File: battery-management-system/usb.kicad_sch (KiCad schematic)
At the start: 20 parts, among them J14 AMPHENOL_micro_usb_10118194-0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, U6 FT230XS

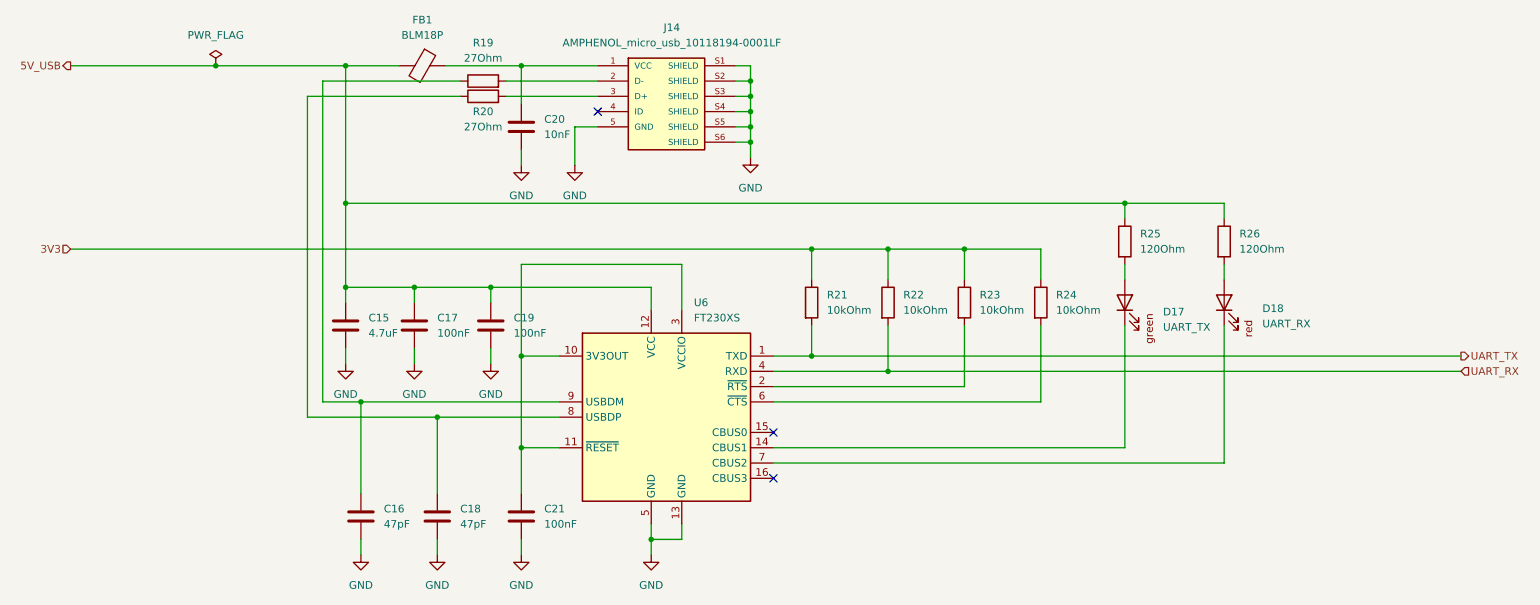
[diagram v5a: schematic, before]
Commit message: add enable input for cell measurement
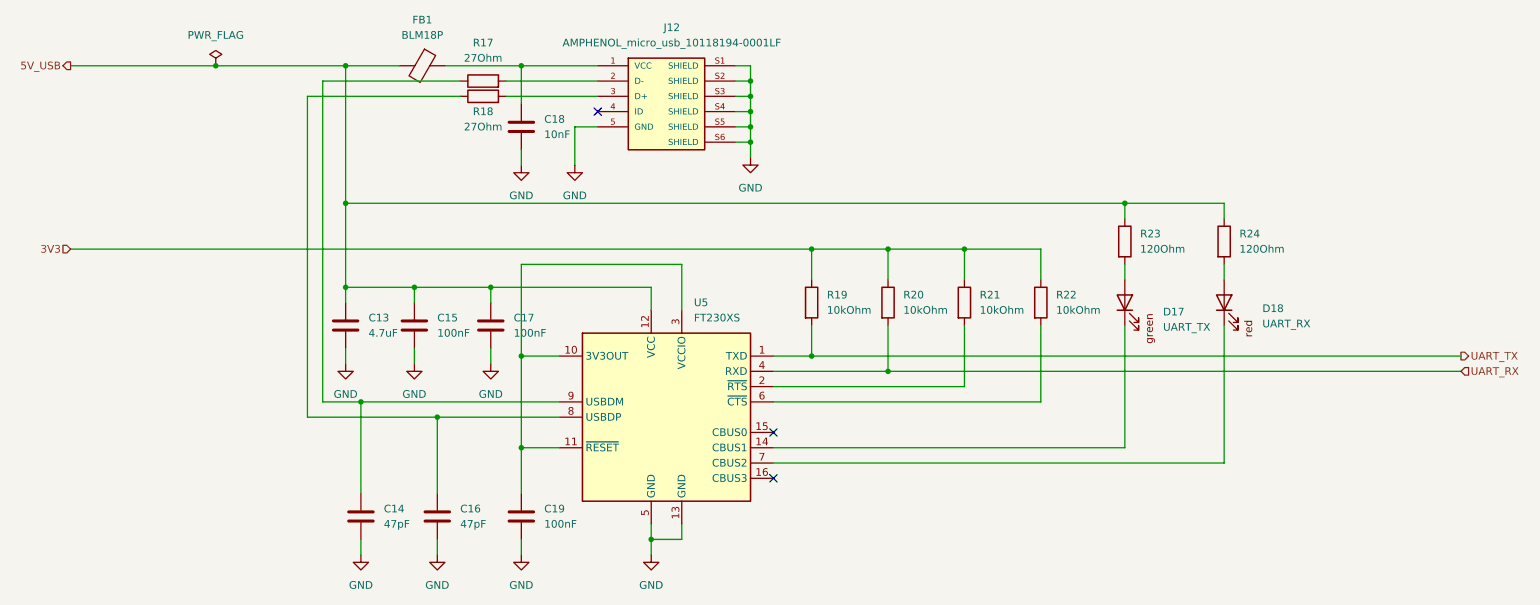
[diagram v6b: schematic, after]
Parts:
- renumbered C15 to C13, C16 to C14, C17 to C15, C18 to C16, C19 to C17, C20 to C18, C21 to C19, J14 to J12, R19 to R17, R20 to R18, R21 to R19, R22 to R20, R23 to R21, R24 to R22, R25 to R23, R26 to R24, U6 to U5
